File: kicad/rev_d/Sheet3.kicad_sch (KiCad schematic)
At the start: 25 parts, among them J10 vg_old

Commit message: pentevo: add reverse-biased diodes to linear regulators
git-svn-id: svn://localhost/local-pentevo@1195 c6c76956-fad2-4150-a3a9-ea0a427205ba
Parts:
- removed C63: 0.1uF, Capacitor_SMD:C_0805_2012Metric_Pad1.18x1.45mm_HandSolder, symbol eva-altium-import:Sheet1_0_CAPCHIP
- removed DA7: LM2903, Package_SO:SOIC-8_3.9x4.9mm_P1.27mm, symbol Comparator:LM2903
- removed DA8: TL431, Package_TO_SOT_SMD:SOT-23_Handsoldering, symbol Reference_Voltage:TL431DBZ
- removed J10: vg_old, symbol Jumper:SolderJumper_2_Open
- removed R150, R173: 1K, Resistor_SMD:R_0805_2012Metric_Pad1.20x1.40mm_HandSolder, symbol Device:R
- removed R154, R155, R166: 10K, Resistor_SMD:R_0805_2012Metric_Pad1.20x1.40mm_HandSolder, symbol Device:R
- removed R156, R162, R168, R169, R170, R174: 47K, Resistor_SMD:R_0805_2012Metric_Pad1.20x1.40mm_HandSolder, symbol Device:R
- removed R167: 2K2, Resistor_SMD:R_0805_2012Metric_Pad1.20x1.40mm_HandSolder, symbol Device:R
- removed R171, R172: 470K, Resistor_SMD:R_0805_2012Metric_Pad1.20x1.40mm_HandSolder, symbol Device:R
- removed VD1, VD13: BAT54C, Package_TO_SOT_SMD:SOT-23_Handsoldering, symbol eva-altium-import:Sheet1_2_BAT54C
- removed VD14, VD15: LL4148, Diode_SMD:D_MiniMELF_Handsoldering, symbol eva-altium-import:Sheet2_0_mirrored_LL4148
- removed VT1: IRLML6402, Package_TO_SOT_SMD:SOT-23_Handsoldering, symbol Transistor_FET:IRLML6402
- removed VT5, VT6: BC847, Package_TO_SOT_SMD:SOT-23_Handsoldering, symbol Transistor_BJT:BC847
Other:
- note removed: "Place only VD1 and solder bridge J10 for no switch"
- note removed: "VG93 12v switcher"

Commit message: pentevo: rev D: start redoing audio part (WIP)
git-svn-id: svn://localhost/local-pentevo@1219 c6c76956-fad2-4150-a3a9-ea0a427205ba
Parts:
- added C116, C41: 0.1uF, C-CHIP, symbol eva-altium-import:Sheet2_3_CAPCHIP
- added C12: 0.1uF, C-CHIP, symbol eva-altium-import:Sheet2_0_CAPCHIP
- added C30, C31, C32, C45: 2.2uF, EC-CHIP, symbol eva-altium-import:Sheet2_2_ECAPCHIP
- added C42, C43, C46, C47, C51, C52, C53, C54: 10uF, EC-CHIP, symbol eva-altium-import:Sheet2_0_ECAPCHIP
- added C44: 820pF NP0, C-CHIP, symbol eva-altium-import:Sheet2_1_CAPCHIP
- added C48, C49: 240pF, C-CHIP, symbol eva-altium-import:Sheet2_0_CAPCHIP
- added C61: 240pF NP0, C-CHIP, symbol eva-altium-import:Sheet2_0_CAPCHIP
- added DA1: NE5532, SO8, symbol eva-altium-import:Sheet2_2_mirrored_NE5532
- added DA9: TLC072, symbol eva-altium-import:TLC072
- added R102: 10K, R-CHIP, symbol eva-altium-import:Sheet2_2_mirrored_RESCHIP
- added R103, R117, R118, R119, R134, R135: 10K, R-CHIP, symbol eva-altium-import:Sheet2_0_RESCHIP
- added R104, R105, R113: 24K, R-CHIP, symbol eva-altium-import:Sheet2_0_RESCHIP
- added R106, R107, R112: 24K, R-CHIP, symbol eva-altium-import:Sheet2_2_mirrored_RESCHIP
- added R108, R109: 51, R-CHIP, symbol eva-altium-import:Sheet2_0_RESCHIP
- added R110, R111: 47K, R-CHIP, symbol eva-altium-import:Sheet2_3_RESCHIP
- added R114: 3K, R-CHIP, symbol eva-altium-import:Sheet2_2_mirrored_RESCHIP
- added R116: 9.1k, R-CHIP, symbol eva-altium-import:Sheet2_0_RESCHIP
- added R120, R121, R122, R133, R136, R137: 47K, R-CHIP, symbol eva-altium-import:Sheet2_0_RESCHIP
- added R138: 10K, R-CHIP, symbol eva-altium-import:Sheet2_3_RESCHIP
- added R141: 10K, R-CHIP, symbol eva-altium-import:Sheet2_2_RESCHIP
- added R86, R99: 20, R-CHIP, symbol eva-altium-import:Sheet2_0_RESCHIP
- added R91, R92, R93: 1K, R-CHIP, symbol eva-altium-import:Sheet2_3_RESCHIP
- added U1: 74HCT1G04, Package_TO_SOT_SMD:SOT-23-5_HandSoldering, symbol 74xGxx:74AHC1G04
- added X10: ST-214C, ST-214C, symbol eva-altium-import:Sheet2_2_ST-214C
- added X14: AAFP/AC97 audio, symbol Connector_Generic_MountingPin:Conn_2Rows-09Pins_MountingPin
- added X16: PLB1-4I, PLB1-4I, symbol eva-altium-import:Sheet2_0_PLB1-4I
- added X17, X18, X20: PLB1-4I, PLB1-4I, symbol eva-altium-import:Sheet2_2_mirrored_PLB1-4I
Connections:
- new net: C52.1, R135.1 (i/o)
- new net: C52.2, R133.2 (i/o1), X18.1 (I/O1)
- new net: C49.1, DA1.6 (-), R103.2 (i/o1), R106.1 (i/o), R107.1 (i/o), R112.1 (i/o), R119.2 (i/o1), R134.2 (i/o1), R141.1 (i/o)
- new net: C30.1, R107.2 (i/o1), R112.2 (i/o1)
- new net: C61.1, DA9.6 (-), R116.1 (i/o), R117.2 (i/o1)
- new net: C45.1, R116.2 (i/o1)
- new net: C31.1, R105.2 (i/o1), R106.2 (i/o1)
- new net: C48.1, DA1.2 (-), R102.2 (i/o1), R104.1 (i/o), R105.1 (i/o), R113.1 (i/o), R118.2 (i/o1), R135.2 (i/o1), R138.1 (i/o)
- new net: C32.1, R104.2 (i/o1), R113.2 (i/o1)
- new net: C48.2, DA1.1 (OUT), R102.1 (i/o), R108.2 (i/o1)
- new net: C46.1, R119.1 (i/o)
- new net: C46.2, R120.2 (i/o1), X17.4 (I/O4)
- new net: C44.2, C45.2, R114.1 (i/o)
- new net: R114.2 (i/o1), U1.4
- new net: C54.1, R138.2 (i/o1)
- new net: C54.2, R136.2 (i/o1), X20.1 (I/O1)
- new net: C53.1, R141.2 (i/o1)
- new net: C53.2, R137.2 (i/o1), X20.4 (I/O4)
- new net: C61.2, R117.1 (i/o), R99.1 (i/o)
- new net: C51.2, R122.2 (i/o1), X18.4 (I/O4)
- new net: C47.1, R118.1 (i/o)
- new net: C47.2, R121.2 (i/o1), X17.1 (I/O1)
- new net: C49.2, DA1.7 (OUT), R103.1 (i/o), R109.2 (i/o1)
- new net: C43.1, R109.1 (i/o)
- new net: C51.1, R134.1 (i/o)
- new net: C42.1, R108.1 (i/o)
- new net: DA9.1, R86.2 (i/o1)
- new net: DA9.7, R99.2 (i/o1)
- new net AVCC5: C12.2, U1.5 (VCC)
- new net AVCC9: C116.1, C41.2, DA9.8 (V+)
- new net AY_CHA: C32.2, R93.2 (i/o1)
- new net AY_CHB: C31.2, R92.2 (i/o1)
- new net AY_CHC: C30.2, R91.2 (i/o1)
- new net BEEP: U1.2
- new net GND: C116.2, C12.1, C41.1, C44.1, DA1.4 (GND), DA1.4 (GND), DA9.4 (V-), R110.1 (i/o), R111.1 (i/o), R120.1 (i/o), R121.1 (i/o), R122.1 (i/o), R133.1 (i/o), R136.1 (i/o), R137.1 (i/o), R91.1 (i/o), R92.1 (i/o), R93.1 (i/o), U1.3 (GND), X10.1, X14.2 (Pin_2), X16.2 (I/O2), X16.3 (I/O3), X17.2 (I/O2), X17.3 (I/O3), X18.2 (I/O2), X18.3 (I/O3), X20.2 (I/O2), X20.3 (I/O3)
- new net LOUT: C42.2, R111.2 (i/o1), X10.5, X14.9 (Pin_9), X16.1 (I/O1)
- new net ROUT: C43.2, R110.2 (i/o1), X10.2, X14.5 (Pin_5), X16.4 (I/O4)
- new net TAPE_IN: X14.1 (Pin_1)
- new net VCCA: DA1.8 (VCCA), DA1.8 (VCCA)
- new net VGND9: DA1.3 (+), DA1.5 (+), DA9.2 (-), DA9.5 (+), R86.1 (i/o)
- new net VGND9_UNBUF: DA9.3 (+)
- no-connect marks 0 -> 7
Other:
- note added: "${##}"
- note added: "${#}"
- note added: "${AUTHOR}"
- note added: "${COMPANY}"
- note added: "${CURRENT_DATE}"
- note added: "${FILENAME}"
- note added: "${REVISION}"
- note added: "${TITLE}"
- note added: "1"
- note added: "2"
- note added: "3"
- note added: "4"
- note added: "A"
- note added: "A2"
- note added: "Audio connections, volume, output"
- note added: "B"
- note added: "C"
- note added: "Company"
- note added: "D"
- note added: "Date"
- note added: "Drawn by"
- note added: "E"
- note added: "F"
- note added: "Filename"
- note added: "Rev"
- note added: "Sheet"
- note added: "Size"
- note added: "Title"
- note added: "YM: 1.35 Vpp AY: 2.00 mA p-p"
- note added: "of"

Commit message: pentevo: rev D: redoing audio (WIP)
git-svn-id: svn://localhost/local-pentevo@1220 c6c76956-fad2-4150-a3a9-ea0a427205ba
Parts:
- removed C116: 0.1uF, C-CHIP, symbol eva-altium-import:Sheet2_3_CAPCHIP
- removed DA1: NE5532, SO8, symbol eva-altium-import:Sheet2_2_mirrored_NE5532
- removed R118, R119, R134, R135: 10K, R-CHIP, symbol eva-altium-import:Sheet2_0_RESCHIP
- removed R138: 10K, R-CHIP, symbol eva-altium-import:Sheet2_3_RESCHIP
- removed R141: 10K, R-CHIP, symbol eva-altium-import:Sheet2_2_RESCHIP
- removed R86, R99: 20, R-CHIP, symbol eva-altium-import:Sheet2_0_RESCHIP
- added C66, C67, C68, C72: 0.1uF, C-CHIP, symbol eva-altium-import:Sheet2_3_CAPCHIP
- added DA1, DA12: TLC072, symbol eva-altium-import:TLC072
- added DA10, DA11: PT2258-S, Package_SO:SO-20_12.8x7.5mm_P1.27mm, symbol Audio:PT2258-S
- C42, C43: value 10uF -> 470uF; footprint EC-CHIP -> (none)
- R108, R109: value 51 -> 20
- R110, R111: value 47K -> 1K
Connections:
- net AVCC9: now also C66.2, C67.1, C68.1, C72.2, DA1.8 (V+), DA10.16 (VCC), DA11.16 (VCC), DA12.8 (V+)
- net GND: now also C66.1, C67.2, C68.2, C72.1, DA1.4 (V-), DA10.14 (GND), DA10.5 (DGND), DA11.14 (GND), DA11.5 (DGND), DA12.4 (V-)
- net VGND9: now also DA9.1, DA1.2 (-), DA1.5 (+), DA10.15 (REF), DA11.15 (REF), DA12.2 (-), DA12.6 (-)
- net EXT2_L: now reaches C52.1
- net EXT2_L: now also DA11.1 (IN1)
- net at C49.1, R103.2 (i/o1), R106.1 (i/o)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: now also DA1.6 (-)
- net at C48.1, R102.2 (i/o1), R104.1 (i/o)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: now also DA1.3 (+)
- net AY_L: now reaches C48.2, R102.1 (i/o)
- net AY_L: now also DA1.1, DA10.1 (IN1); no longer R108.2 (i/o1)
- net EXT1_R: now reaches C46.1
- net EXT1_R: now also DA10.10 (IN6)
- net EXT3_L: now reaches C54.1
- net EXT3_L: now also DA11.3 (IN3)
- net at C54.2, X20.1 (I/O1): now also R137.2 (i/o1); no longer R136.2 (i/o1)
- net EXT3_R: now reaches C53.1
- net EXT3_R: now also DA11.8 (IN4)
- net at C53.2, X20.4 (I/O4): now also R136.2 (i/o1); no longer R137.2 (i/o1)
- net BEEP_LR: now reaches C61.2, R117.1 (i/o)
- net BEEP_LR: now also DA9.7, DA10.3 (IN3), DA10.8 (IN4)
- net EXT1_L: now reaches C47.1
- net EXT1_L: now also DA10.9 (IN5)
- net AY_R: now reaches C49.2, R103.1 (i/o)
- net AY_R: now also DA1.7, DA10.2 (IN2); no longer R109.2 (i/o1)
- net EXT2_R: now reaches C51.1
- net EXT2_R: now also DA11.2 (IN2)
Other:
- note added: "YM: 1.35 V p-p AY: 2.00 mA p-p"
- note removed: "YM: 1.35 Vpp AY: 2.00 mA p-p"
- moved on the sheet: C41, C42, C43, C46, C47, C51, C52, C53, C54, DA9C, R108, R109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

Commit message: pentevo: rev D: redoing audio (WIP), add reverse diodes to linear regulators
git-svn-id: svn://localhost/local-pentevo@1221 c6c76956-fad2-4150-a3a9-ea0a427205ba
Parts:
- added C116, C117, C118: 0.1uF, C-CHIP, symbol eva-altium-import:Sheet2_3_CAPCHIP
- added C119: 10uF, EC-CHIP, symbol eva-altium-import:Sheet2_3_ECAPCHIP
- added C120, C121, C75, C95: 240pF NP0, C-CHIP, symbol eva-altium-import:Sheet2_0_CAPCHIP
- added DA13: TLC072, symbol eva-altium-import:TLC072
- added DA14: TPA6120, symbol eva-altium-import:TPA6120
- added DA15: TL431, Package_TO_SOT_SMD:SOT-23_Handsoldering, symbol Reference_Voltage:TL431DBZ
- added R118, R119, R134, R135, R138, R141, R145, R156, R166, R170, R86, R99: 10K, R-CHIP, symbol eva-altium-import:Sheet2_2_mirrored_RESCHIP
- added R171, R172, R173, R182, R183: 1K, R-CHIP, symbol eva-altium-import:Sheet2_0_RESCHIP
- added R174: 1K5, R-CHIP, symbol eva-altium-import:Sheet2_0_RESCHIP
- added R177: 2K2, R-CHIP, symbol eva-altium-import:Sheet2_0_RESCHIP
- added R178: 47K, R-CHIP, symbol eva-altium-import:Sheet2_0_RESCHIP
- added R179, R180, R181: 10K, R-CHIP, symbol eva-altium-import:Sheet2_3_RESCHIP
- added VD19: US1A, Diode_SMD:D_SMA, symbol Diode:US1A
- C48, C49: value 240pF -> 240pF NP0
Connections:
- net GND: now also C116.1, C117.1, C118.1, C119.2, DA13.4 (V-), DA14.1 (V-), DA14.20 (V-), DA15.3 (A), R174.2 (i/o1)
- net VGND9: now also DA1.3 (+), DA12.3 (+), DA12.5 (+); no longer DA1.2 (-), DA12.2 (-), DA12.6 (-)
- net at DA11.10 (IN6): now also DA12.7, C95.2, R99.1 (i/o)
- net at DA11.11 (OUT6): now also R183.2 (i/o1)
- net at DA11.12 (OUT5): now also R182.2 (i/o1)
- net at DA11.13 (OUT4): now also R145.2 (i/o1)
- net at DA11.18 (OUT3): now also R118.2 (i/o1)
- net at DA11.19 (OUT2): now also R156.2 (i/o1)
- net at DA11.20 (OUT1): now also R134.2 (i/o1)
- net at DA11.9 (IN5): now also DA12.1, C75.2, R86.1 (i/o)
- net at C48.1, R102.2 (i/o1), R104.1 (i/o)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: now also DA1.2 (-); no longer DA1.3 (+)
- net at C43.1, R109.1 (i/o): now also R180.2 (i/o1)
- net at R109.2 (i/o1): now also DA14.19, R172.1 (i/o)
- net at C42.1, R108.1 (i/o): now also R181.2 (i/o1)
- net at R108.2 (i/o1): now also DA14.2, R171.1 (i/o)
- net at DA10.11 (OUT6): now also R166.2 (i/o1)
- net at DA10.12 (OUT5): now also R135.2 (i/o1)
- net at DA10.13 (OUT4): now also R170.2 (i/o1)
- net at DA10.18 (OUT3): now also R138.2 (i/o1)
- net at DA10.19 (OUT2): now also R119.2 (i/o1)
- net at DA10.20 (OUT1): now also R141.2 (i/o1)
- new net: C121.1, DA13.2 (-), R180.1 (i/o)
- new net: C121.2, DA13.1, DA14.17 (+)
- new net: DA15.1 (K), R173.2 (i/o1), R177.1 (i/o), R178.1 (i/o), R179.1 (i/o)
- new net: DA15.2 (REF), R174.1 (i/o), R177.2 (i/o1), R178.2 (i/o1)
- new net: C95.1, DA12.6 (-), R119.1 (i/o), R145.1 (i/o), R156.1 (i/o), R166.1 (i/o), R170.1 (i/o), R99.2 (i/o1)
- new net: C75.1, DA12.2 (-), R118.1 (i/o), R134.1 (i/o), R135.1 (i/o), R138.1 (i/o), R141.1 (i/o), R86.2 (i/o1)
- new net: C120.1, DA13.6 (-), R181.1 (i/o)
- new net: C120.2, DA13.7, DA14.4 (+)
- new net: DA14.5 (-), R171.2 (i/o1)
- new net: DA14.16 (-), R172.2 (i/o1)
- new net AVCC12: C116.2, C117.2, C118.2, DA13.8 (V+), DA14.18 (V+), DA14.3 (V+), R173.1 (i/o), VD19.1 (K)
- new net VGND12: C119.1, DA13.3 (+), DA13.5 (+), R179.2 (i/o1), VD19.2 (A)
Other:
- moved on the sheet: C66, C72, DA12C, DA1C, DA9A, X14

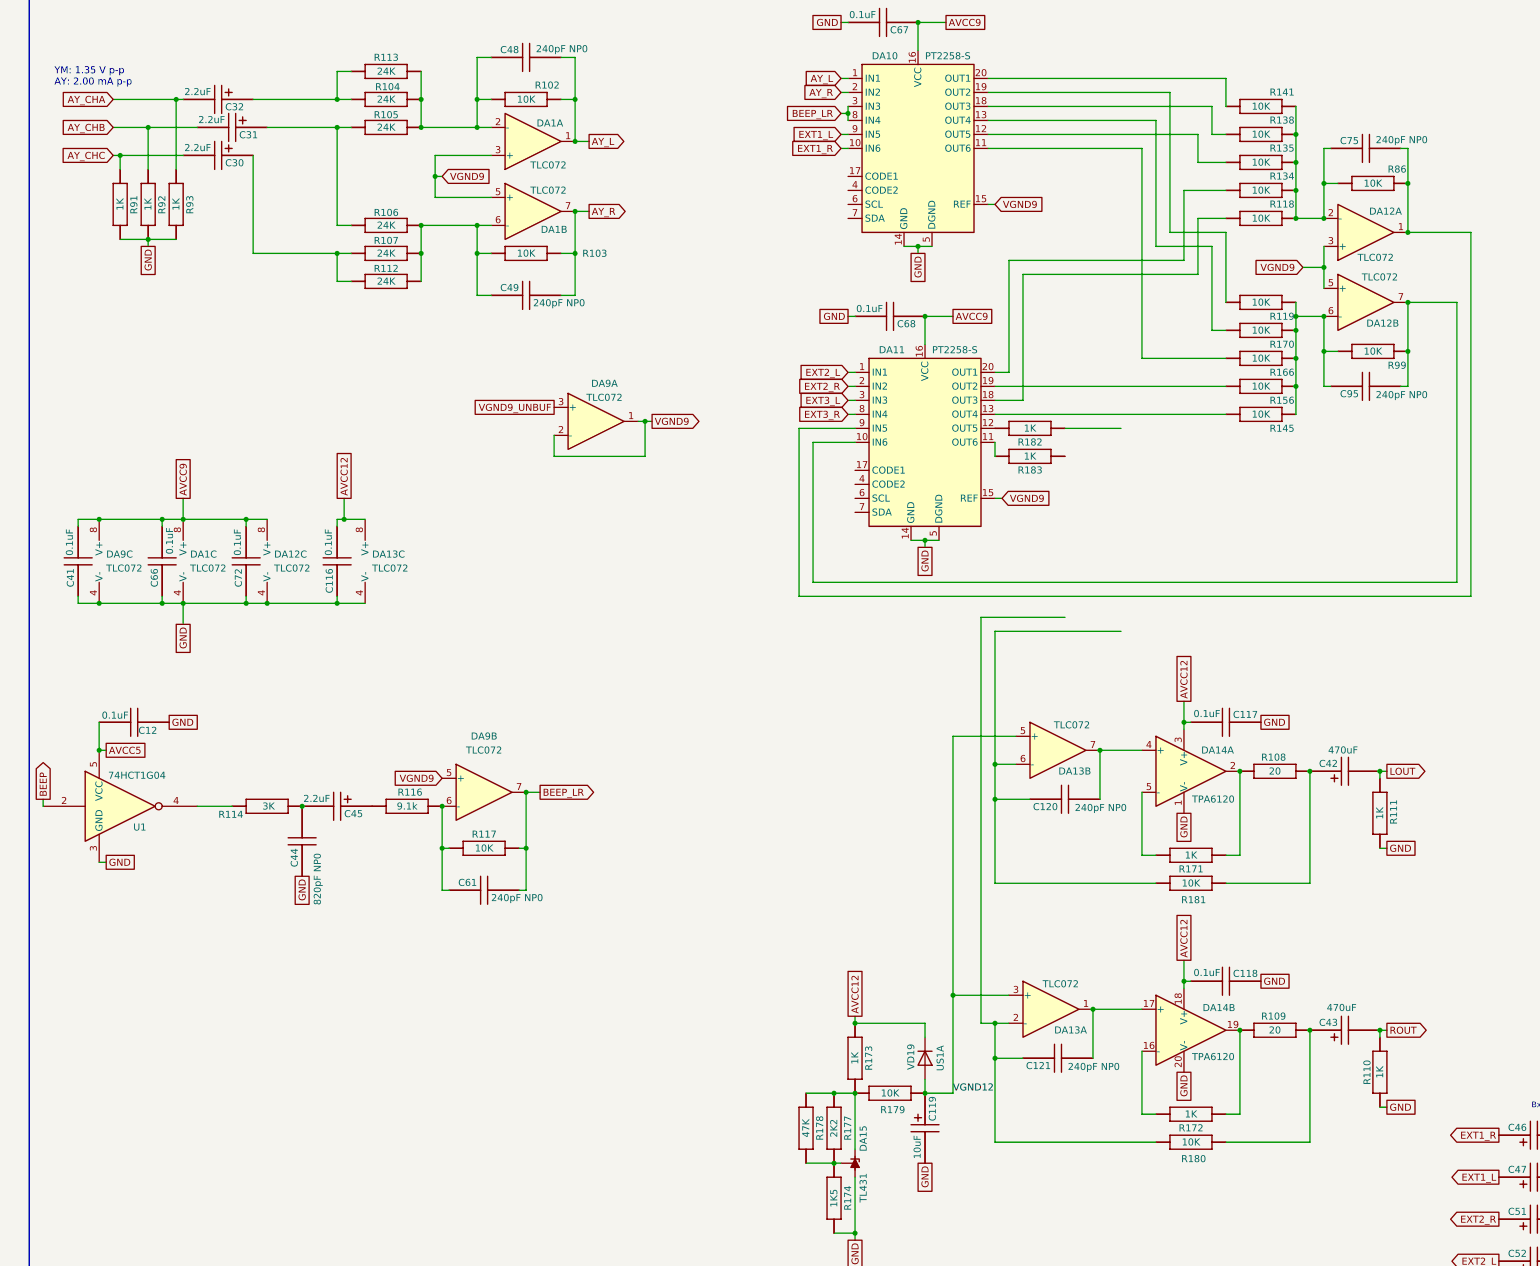
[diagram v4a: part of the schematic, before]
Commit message: pentevo: rev D: start redoing audio part (WIP)
git-svn-id: svn://localhost/local-pentevo@1222 c6c76956-fad2-4150-a3a9-ea0a427205ba
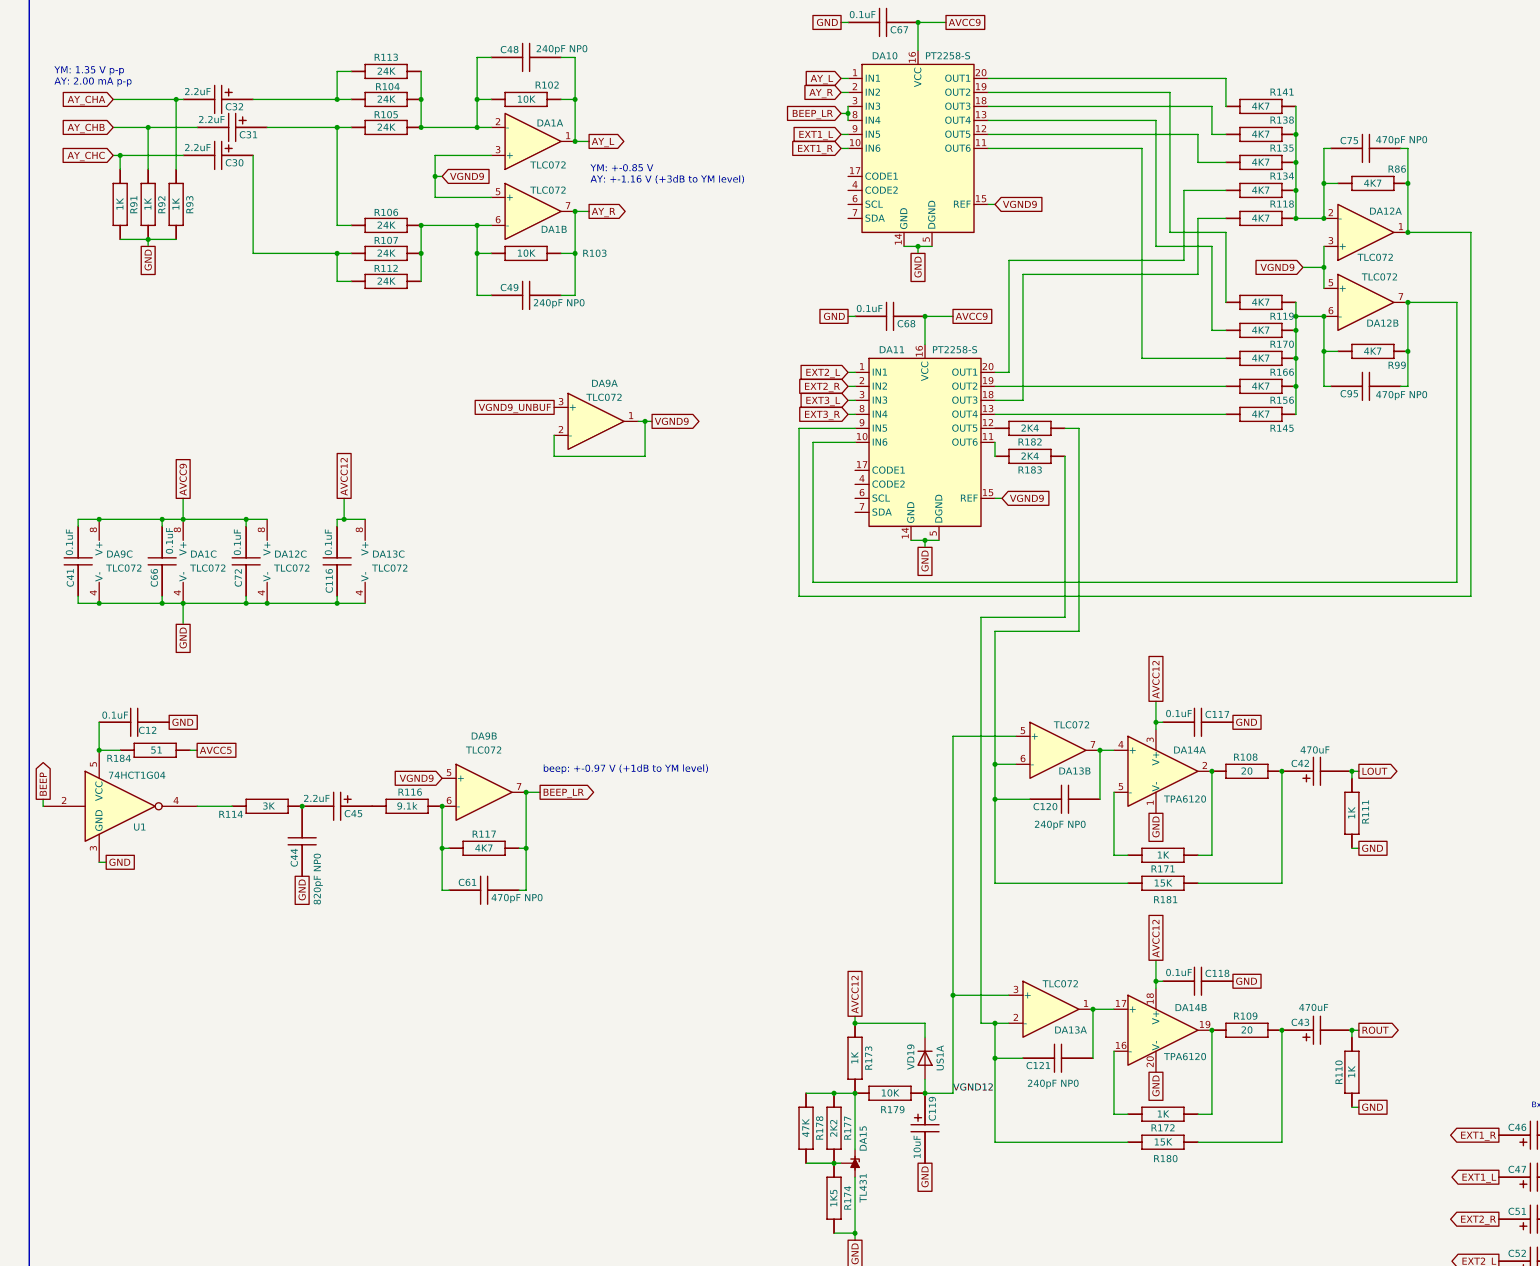
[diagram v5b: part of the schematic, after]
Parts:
- added R184: 51, R-CHIP, symbol eva-altium-import:Sheet2_2_mirrored_RESCHIP
- C61, C75, C95: value 240pF NP0 -> 470pF NP0
- R117, R118, R119, R134, R135, R138, R141, R145, R156, R166, R170, R86, R99: value 10K -> 4K7
- R180, R181: value 10K -> 15K
- R182, R183: value 1K -> 2K4
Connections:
- net AVCC5: now also R184.1 (i/o); no longer C12.2, U1.5 (VCC)
- net at C121.1, DA13.2 (-), R180.1 (i/o): now also R183.1 (i/o)
- net at C120.1, DA13.6 (-), R181.1 (i/o): now also R182.1 (i/o)
- new net: C12.2, R184.2 (i/o1), U1.5 (VCC)
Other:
- note added: "YM: +-0.85 V AY: +-1.16 V (+3dB to YM level)"
- note added: "beep: +-0.97 V (+1dB to YM level)"
- moved on the sheet: C117, C118, C42, C43, DA14A, DA14B, R108, R109, R110, R111, R171, R172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
